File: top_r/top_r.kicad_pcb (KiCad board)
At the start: 2 copper layers, 128.4 x 119.3 mm, 31 parts, among them SW29 SW_Push, SW30 SW_Push, SW31 SW_Push, SW32 SW_Push, SW33 SW_Push, SW34 SW_Push, SW35 SW_Push, SW36 SW_Push, SW37 SW_Push, SW38 SW_Push, SW39 SW_Push, SW40 SW_Push, SW41 SW_Push, SW42 SW_Push, SW43 SW_Push, SW44 SW_Push, SW45 SW_Push, SW46 SW_Push, SW47 SW_Push, SW48 SW_Push, SW49 SW_Push, SW50 SW_Push, SW51 SW_Push, SW52 SW_Push, SW53 SW_Push, SW54 SW_Push, SW55 SW_Push

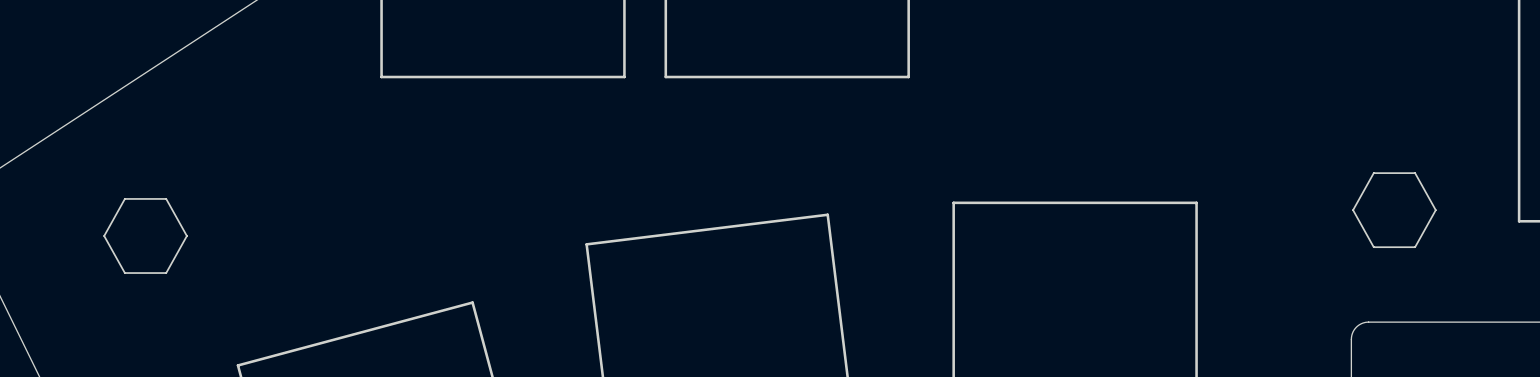
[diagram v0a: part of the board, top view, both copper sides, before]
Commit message: feat: add hole to switch plate
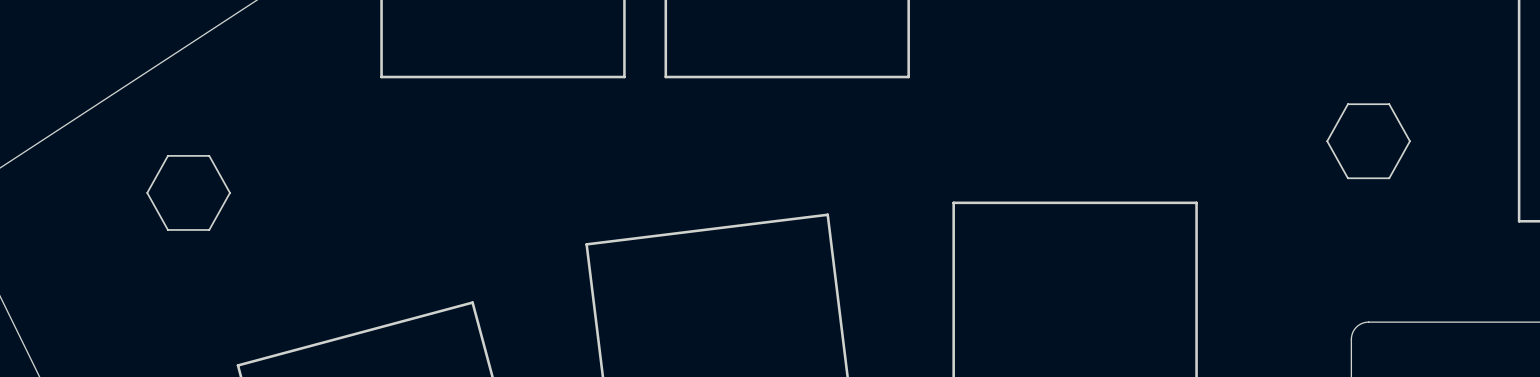
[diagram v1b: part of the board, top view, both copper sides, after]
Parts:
- moved Ref** 4.27 mm to (169.5, 121.0)
- moved Ref** 3.54 mm to (101.0, 124.0)
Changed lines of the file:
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@@
 	(footprint "kbd_Hole:m2_Spacer_Hole_hex"
 		(layer "F.Cu")
-		(at 98.5 126.5)
+		(at 101 124)
 		(descr "Mounting Hole 2.2mm, no annular, M2")
 		(tags "mounting hole 2.2mm no annular m2")
@@
 	(footprint "kbd_Hole:m2_Spacer_Hole_hex"
 		(layer "F.Cu")
-		(at 171 125)
+		(at 169.5 121)
 		(descr "Mounting Hole 2.2mm, no annular, M2")
 		(tags "mounting hole 2.2mm no annular m2")
